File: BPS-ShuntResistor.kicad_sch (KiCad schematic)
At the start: 9 parts, among them J1 Amp_Conn, J2 Conn_01x01_Female, J3 Conn_01x01_Female

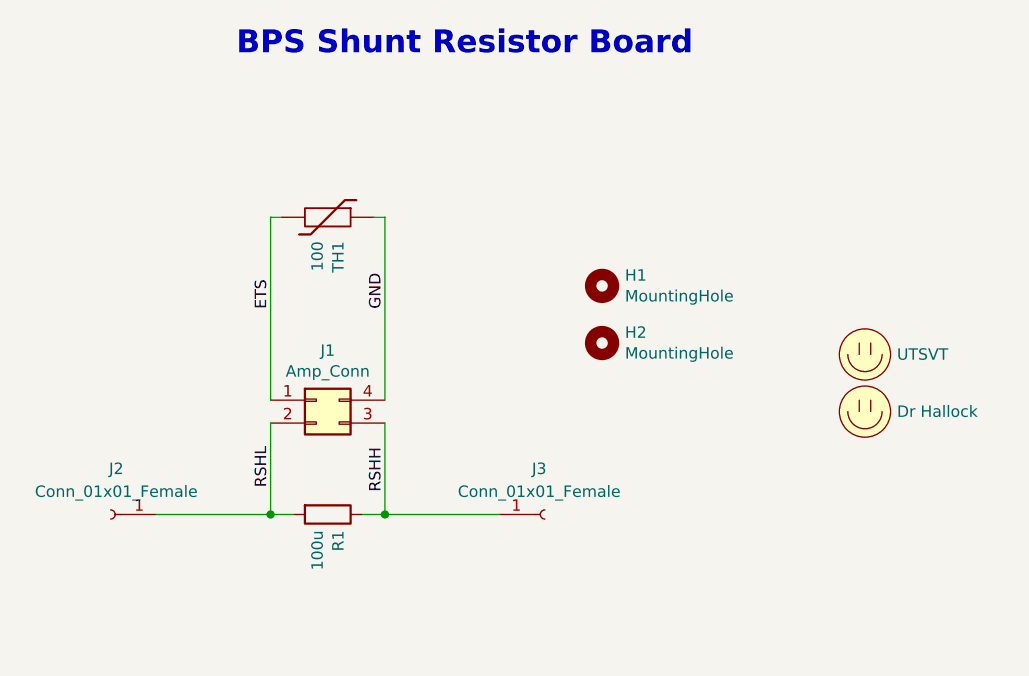
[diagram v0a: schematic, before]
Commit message: working on voltage divider - better resolution; need to make footprint for the shunt resistor proper
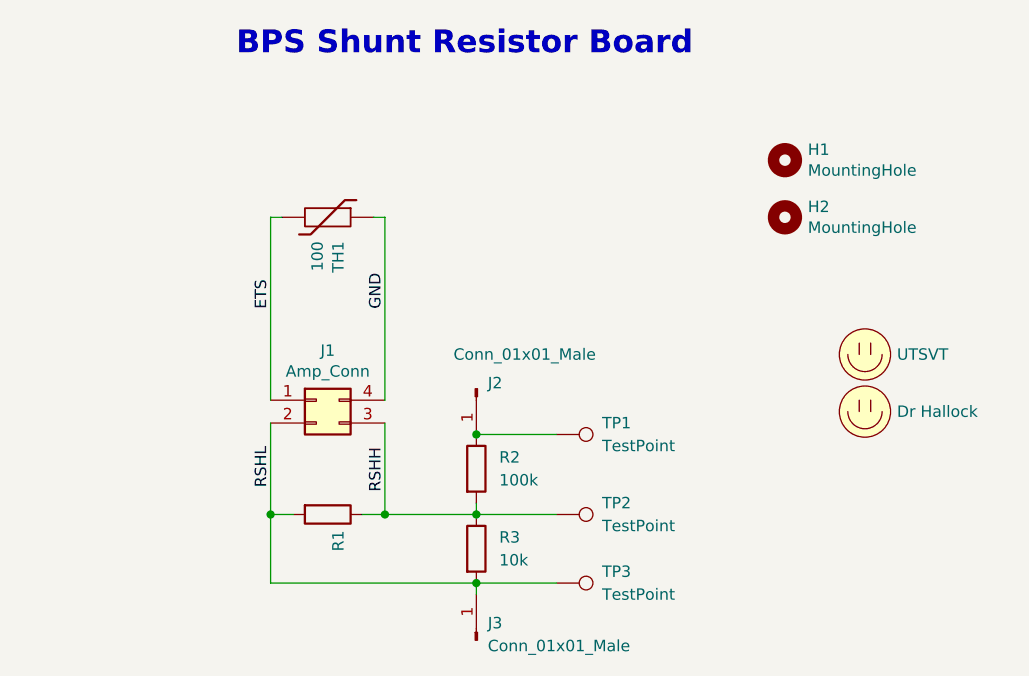
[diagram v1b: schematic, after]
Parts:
- removed J2, J3: Conn_01x01_Female, Connector:Banana_Jack_1Pin, symbol Connector:Conn_01x01_Female
- added J2, J3: Conn_01x01_Male, Connector_PinHeader_2.54mm:PinHeader_1x01_P2.54mm_Vertical, symbol Connector:Conn_01x01_Male
- added R2: 100k, Resistor_SMD:R_0805_2012Metric, symbol Device:R
- added R3: 10k, Resistor_SMD:R_0805_2012Metric, symbol Device:R
- added TP1, TP2, TP3: TestPoint, TestPoint:TestPoint_Pad_2.5x2.5mm, symbol Connector:TestPoint
- R1: value 100u -> (none); footprint UTSVT_Passive:Power_Metal_Strip_Battery_Shunt_Resistor -> (none)
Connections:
- net RSHH: now also R2.2, R3.1, TP2.1
- net RSHL: now also J3.1 (Pin_1), R3.2, TP3.1
- new net: J2.1 (Pin_1), R2.1, TP1.1
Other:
- moved on the sheet: H1, H2

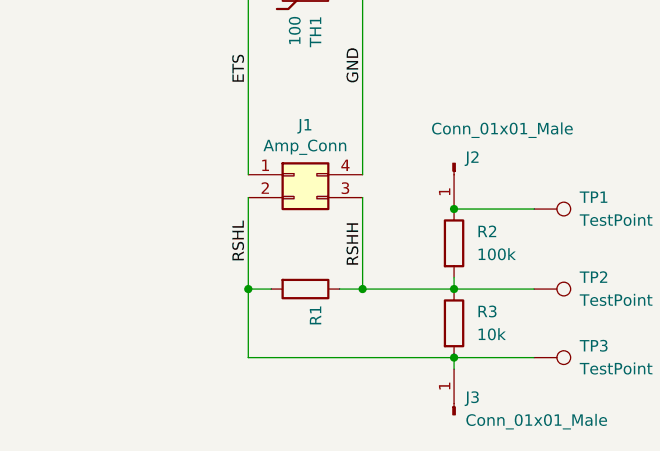
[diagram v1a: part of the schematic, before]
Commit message: working on new footprint for shunt resistor
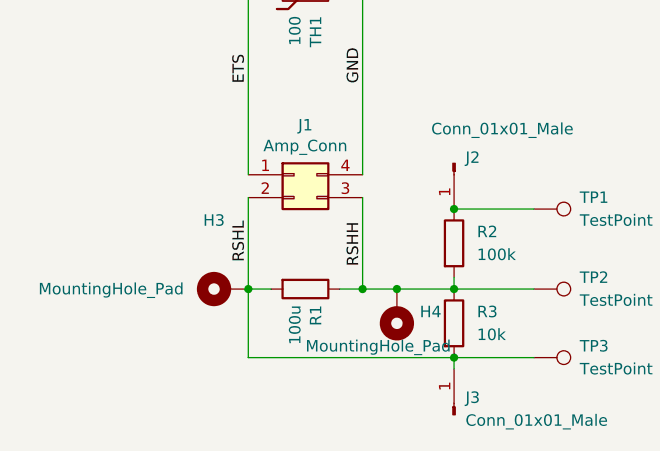
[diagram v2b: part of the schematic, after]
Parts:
- added H3, H4: MountingHole_Pad, symbol Mechanical:MountingHole_Pad
- R1: value (none) -> 100u; footprint (none) -> UTSVT_Passive:Vishay_Shunt_Resistor_100u
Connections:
- net RSHH: now also H4.1
- net RSHL: now also H3.1
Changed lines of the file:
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@@
   (junction (at 152.4 114.3) (diameter 0) (color 0 0 0 0)
   )
+  (junction (at 146.05 123.19) (diameter 0) (color 0 0 0 0)
+  )
   (junction (at 129.54 123.19) (diameter 0) (color 0 0 0 0)
   )
@@
   (junction (at 152.4 130.81) (diameter 0) (color 0 0 0 0)
   )
-  (wire (pts (xy 142.24 123.19) (xy 152.4 123.19))
+  (wire (pts (xy 146.05 123.19) (xy 152.4 123.19))
+    (stroke (width 0) (type default) (color 0 0 0 0))
+  )
+  (wire (pts (xy 142.24 123.19) (xy 146.05 123.19))
     (stroke (width 0) (type default) (color 0 0 0 0))
   )
@@
       (effects (font (size 1.27 1.27)) (justify left))
     )
-    (property "Value" "" (id 1) (at 134.747 124.968 0)
-      (effects (font (size 1.27 1.27)) (justify left))
-    )
-    (property "Footprint" "" (id 2) (at 135.89 121.412 90)
+    (property "Value" "100u" (id 1) (at 134.747 124.968 0)
+      (effects (font (size 1.27 1.27)) (justify left))
+    )
+    (property "Footprint" "UTSVT_Passive:Vishay_Shunt_Resistor_100u" (id 2) (at 135.89 121.412 90)
       (effects (font (size 1.27 1.27)) hide)
     )
@@
     )
   )
+  (symbol (lib_id "Mechanical:MountingHole_Pad") (at 146.05 125.73 180) (unit 1)
+    (in_bom yes) (on_board yes)
+    (property "Reference" "H4" (id 0) (at 148.59 125.7299 0)
+      (effects (font (size 1.27 1.27)) (justify right))
+    )
+    (property "Value" "MountingHole_Pad" (id 1) (at 135.89 129.54 0)
+      (effects (font (size 1.27 1.27)) (justify right))
+    )
+    (property "Footprint" "" (id 2) (at 146.05 125.73 0)
+      (effects (font (size 1.27 1.27)) hide)
+    )
+    (property "Datasheet" "~" (id 3) (at 146.05 125.73 0)
+      (effects (font (size 1.27 1.27)) hide)
+    )
+    (pin "1")
+  )
   (symbol (lib_id "Connector:Conn_01x01_Male") (at 152.4 137.16 90) (unit 1)
     (in_bom yes) (on_board yes) (fields_autoplaced)
@@
     )
     (property "Datasheet" "~" (id 3) (at 152.4 109.22 0)
+      (effects (font (size 1.27 1.27)) hide)
+    )
+    (pin "1")
+  )
+  (symbol (lib_id "Mechanical:MountingHole_Pad") (at 127 123.19 90) (unit 1)
+    (in_bom yes) (on_board yes)
+    (property "Reference" "H3" (id 0) (at 125.73 115.57 90))
+    (property "Value" "MountingHole_Pad" (id 1) (at 114.3 123.19 90))
+    (property "Footprint" "" (id 2) (at 127 123.19 0)
+      (effects (font (size 1.27 1.27)) hide)
+    )
+    (property "Datasheet" "~" (id 3) (at 127 123.19 0)
       (effects (font (size 1.27 1.27)) hide)
     )
@@
       (reference "H2") (unit 1) (value "MountingHole") (footprint "MountingHole:MountingHole_2.7mm_M2.5")
     )
+    (path "/9246bb10-5275-45bd-a3fe-52fd6dfd26be"
+      (reference "H3") (unit 1) (value "MountingHole_Pad") (footprint "")
+    )
+    (path "/0cc767f7-323e-46de-a29a-08ff62fdd107"
+      (reference "H4") (unit 1) (value "MountingHole_Pad") (footprint "")
+    )
     (path "/00000000-0000-0000-0000-00005f55aec1"
       (reference "J1") (unit 1) (value "Amp_Conn") (footprint "UTSVT_Connectors:Power_Metal_Strip_Battery_Shunt_Resistor_4_Pin_Connector")
@@
     )
     (path "/00000000-0000-0000-0000-00005f548200"
-      (reference "R1") (unit 1) (value "100u") (footprint "Resistor_SMD:R_Shunt_Vishay_WSR2_WSR3")
+      (reference "R1") (unit 1) (value "100u") (footprint "UTSVT_Passive:Vishay_Shunt_Resistor_100u")
     )
     (path "/57106b0f-d7e1-4ac5-a294-9d97579b9daf"

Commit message: trying to figure out the schematic
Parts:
- removed H3, H4: MountingHole_Pad, symbol Mechanical:MountingHole_Pad
- R2: value 100k -> R
- R3: value 10k -> R
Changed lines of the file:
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@@
   (junction (at 152.4 114.3) (diameter 0) (color 0 0 0 0)
   )
-  (junction (at 146.05 123.19) (diameter 0) (color 0 0 0 0)
-  )
   (junction (at 129.54 123.19) (diameter 0) (color 0 0 0 0)
   )
@@
   (junction (at 152.4 130.81) (diameter 0) (color 0 0 0 0)
   )
-  (wire (pts (xy 146.05 123.19) (xy 152.4 123.19))
-    (stroke (width 0) (type default) (color 0 0 0 0))
-  )
-  (wire (pts (xy 142.24 123.19) (xy 146.05 123.19))
+  (wire (pts (xy 142.24 123.19) (xy 152.4 123.19))
     (stroke (width 0) (type default) (color 0 0 0 0))
   )
@@
     )
   )
-  (symbol (lib_id "Mechanical:MountingHole_Pad") (at 146.05 125.73 180) (unit 1)
-    (in_bom yes) (on_board yes)
-    (property "Reference" "H4" (id 0) (at 148.59 125.7299 0)
-      (effects (font (size 1.27 1.27)) (justify right))
-    )
-    (property "Value" "MountingHole_Pad" (id 1) (at 135.89 129.54 0)
-      (effects (font (size 1.27 1.27)) (justify right))
-    )
-    (property "Footprint" "" (id 2) (at 146.05 125.73 0)
-      (effects (font (size 1.27 1.27)) hide)
-    )
-    (property "Datasheet" "~" (id 3) (at 146.05 125.73 0)
-      (effects (font (size 1.27 1.27)) hide)
-    )
-    (pin "1")
-  )
   (symbol (lib_id "Connector:Conn_01x01_Male") (at 152.4 137.16 90) (unit 1)
     (in_bom yes) (on_board yes) (fields_autoplaced)
@@
       (effects (font (size 1.27 1.27)) (justify left))
     )
-    (property "Value" "100k" (id 1) (at 154.94 119.3799 0)
+    (property "Value" "R" (id 1) (at 154.94 119.3799 0)
       (effects (font (size 1.27 1.27)) (justify left))
     )
@@
     (pin "1")
   )
-  (symbol (lib_id "Mechanical:MountingHole_Pad") (at 127 123.19 90) (unit 1)
-    (in_bom yes) (on_board yes)
-    (property "Reference" "H3" (id 0) (at 125.73 115.57 90))
-    (property "Value" "MountingHole_Pad" (id 1) (at 114.3 123.19 90))
-    (property "Footprint" "" (id 2) (at 127 123.19 0)
-      (effects (font (size 1.27 1.27)) hide)
-    )
-    (property "Datasheet" "~" (id 3) (at 127 123.19 0)
-      (effects (font (size 1.27 1.27)) hide)
-    )
-    (pin "1")
-  )
   (symbol (lib_id "Connector:TestPoint") (at 161.29 130.81 270) (unit 1)
     (in_bom yes) (on_board yes) (fields_autoplaced)
@@
       (effects (font (size 1.27 1.27)) (justify left))
     )
-    (property "Value" "10k" (id 1) (at 154.94 128.2699 0)
+    (property "Value" "R" (id 1) (at 154.94 128.2699 0)
       (effects (font (size 1.27 1.27)) (justify left))
     )
@@
       (reference "H2") (unit 1) (value "MountingHole") (footprint "MountingHole:MountingHole_2.7mm_M2.5")
     )
-    (path "/9246bb10-5275-45bd-a3fe-52fd6dfd26be"
-      (reference "H3") (unit 1) (value "MountingHole_Pad") (footprint "")
-    )
-    (path "/0cc767f7-323e-46de-a29a-08ff62fdd107"
-      (reference "H4") (unit 1) (value "MountingHole_Pad") (footprint "")
-    )
     (path "/00000000-0000-0000-0000-00005f55aec1"
       (reference "J1") (unit 1) (value "Amp_Conn") (footprint "UTSVT_Connectors:Power_Metal_Strip_Battery_Shunt_Resistor_4_Pin_Connector")
@@
     )
     (path "/57106b0f-d7e1-4ac5-a294-9d97579b9daf"
-      (reference "R2") (unit 1) (value "100k") (footprint "Resistor_SMD:R_0805_2012Metric")
+      (reference "R2") (unit 1) (value "R") (footprint "Resistor_SMD:R_0805_2012Metric")
     )
     (path "/c8cbe576-bc4c-4776-ba66-7b99c7984f21"
-      (reference "R3") (unit 1) (value "10k") (footprint "Resistor_SMD:R_0805_2012Metric")
+      (reference "R3") (unit 1) (value "R") (footprint "Resistor_SMD:R_0805_2012Metric")
     )
     (path "/00000000-0000-0000-0000-00005f548caa"

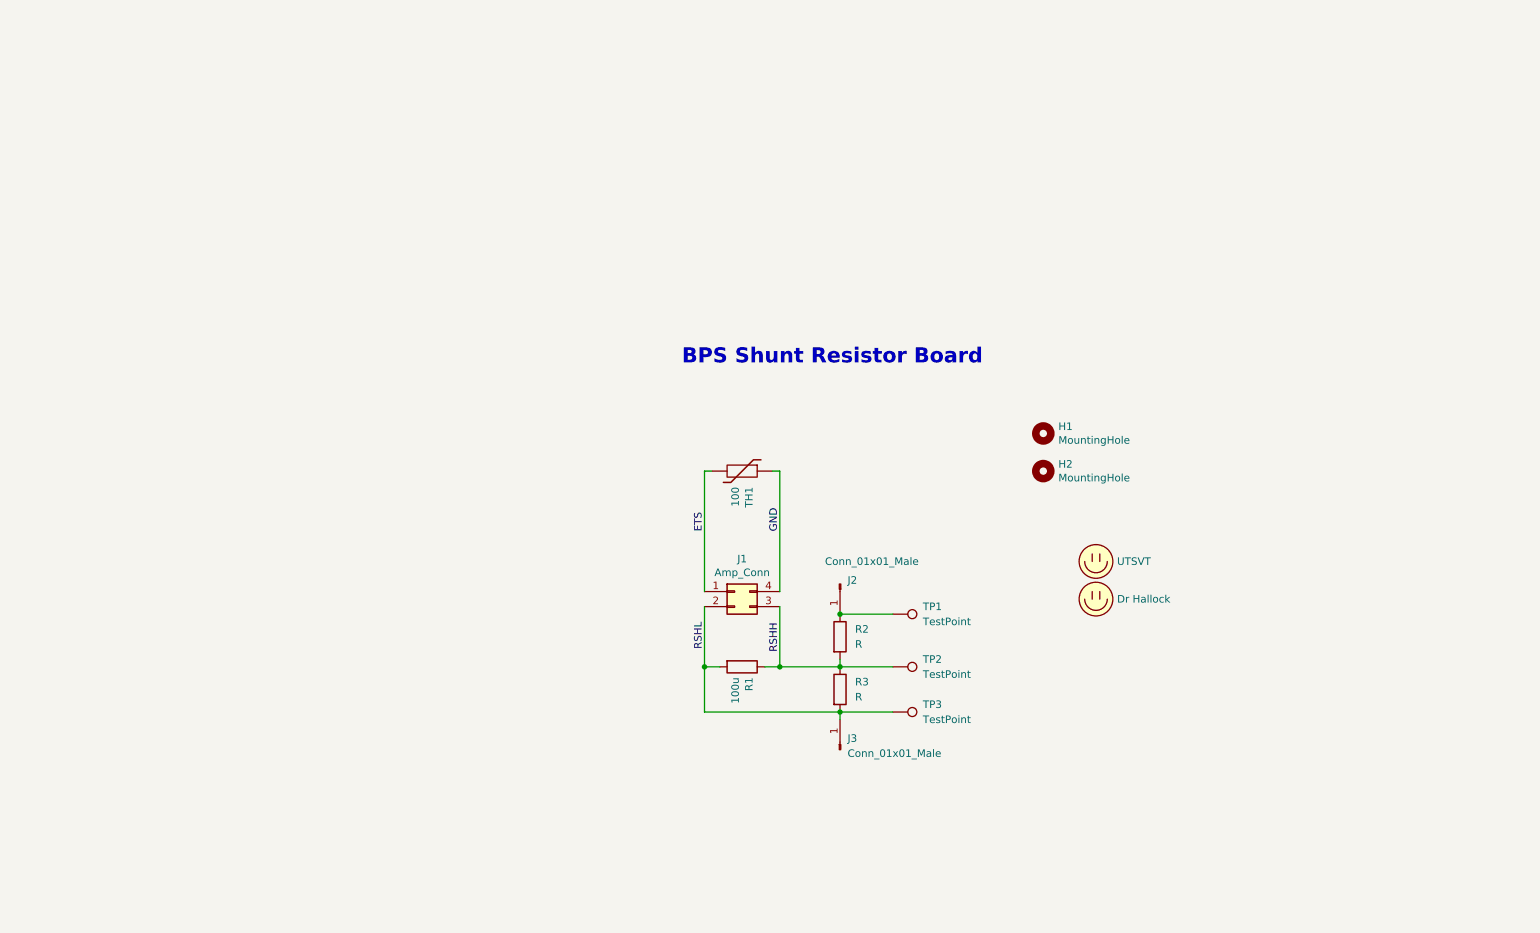
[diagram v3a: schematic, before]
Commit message: Adding voltage divider for tests
Net labels to allow voltage divider/shunt resistor to all work properly.

Voltage divider stays separate from the shunt itself, but divides down to the shunt resistor voltage levels, such that we can route the voltage divider values directly into the current monitor.
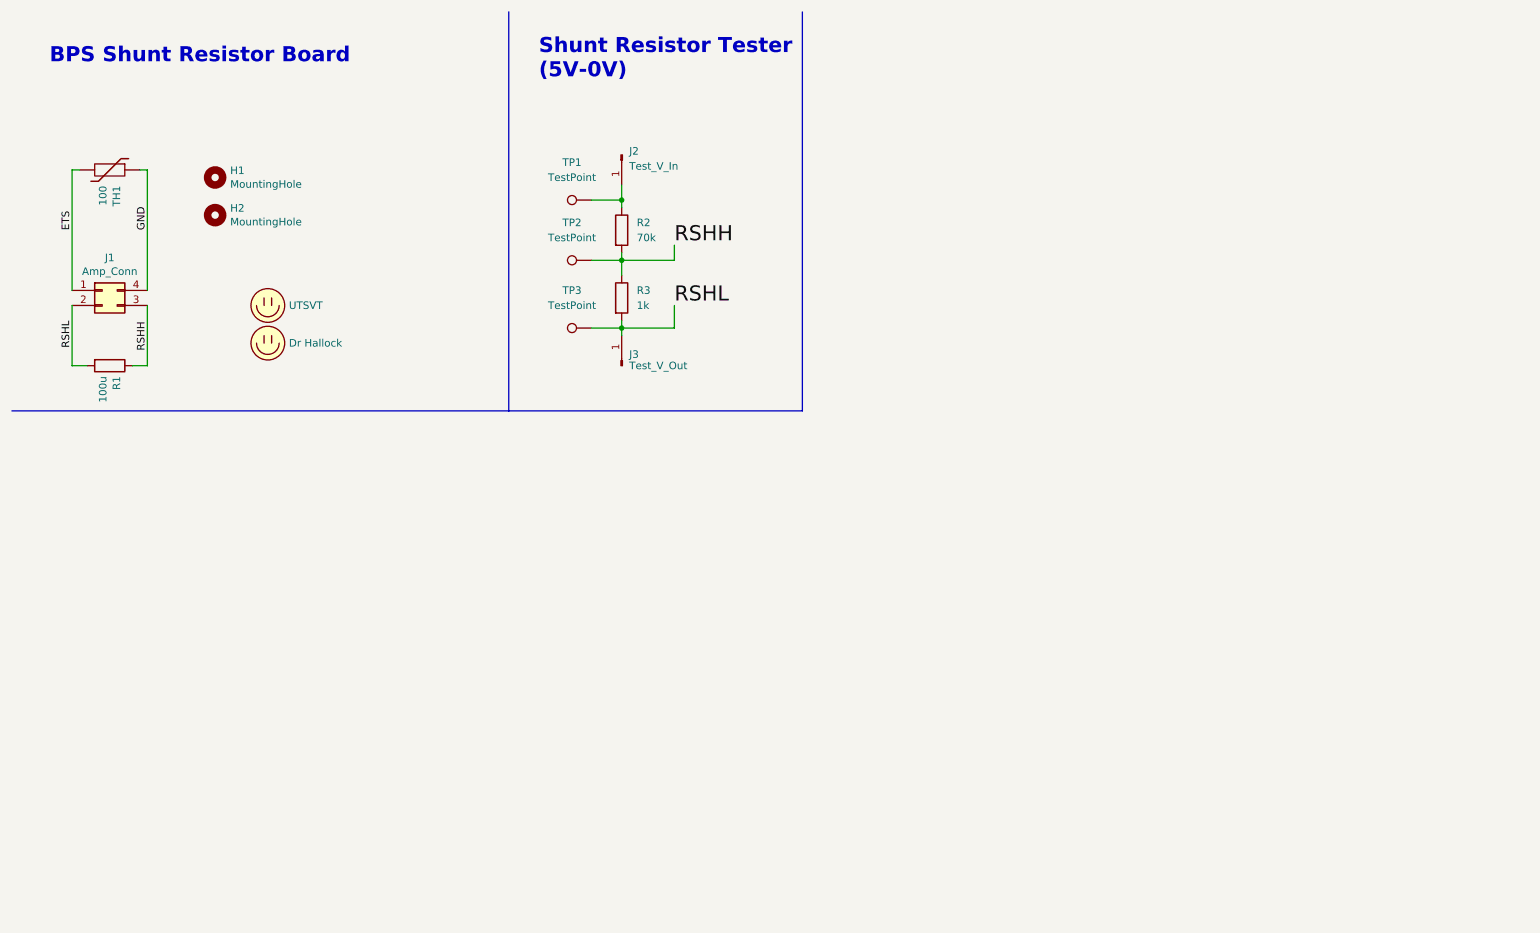
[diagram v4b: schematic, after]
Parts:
- J2: value Conn_01x01_Male -> Test_V_In
- J3: value Conn_01x01_Male -> Test_V_Out
- R2: value R -> 70k
- R3: value R -> 1k
- TP1, TP2, TP3: footprint TestPoint:TestPoint_Pad_2.5x2.5mm -> TestPoint:TestPoint_Bridge_Pitch3.81mm_Drill1.3mm
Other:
- note added: "Shunt Resistor Tester (5V-0V)"
- moved on the sheet: H1, H2, J1, R1, TH1
